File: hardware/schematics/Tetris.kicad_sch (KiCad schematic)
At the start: 13 parts, among them SW1 BTN UP, SW2 BTN RIGHT, SW3 BTN DOWN, SW4 BTN LEFT, SW5 ON/OFF Switch

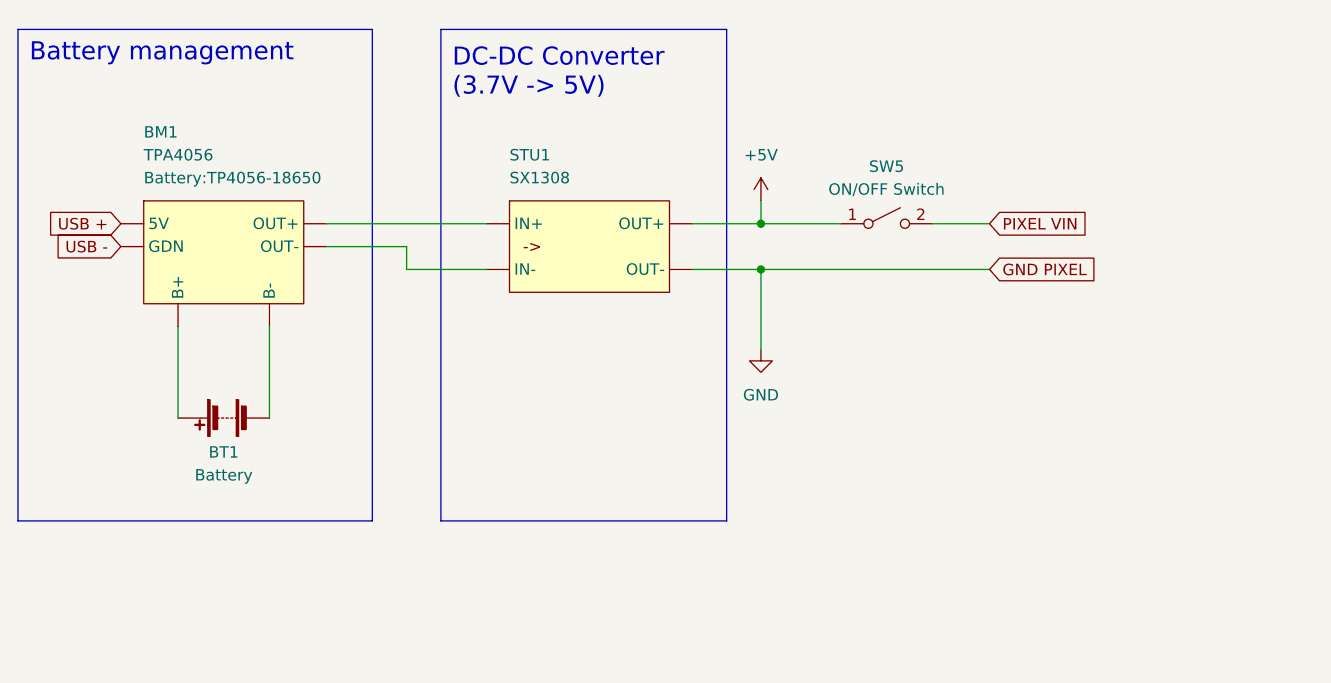
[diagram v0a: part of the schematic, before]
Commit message: Corrected schematics
Moved ON/OFF switch between battery and the DC-DC converter
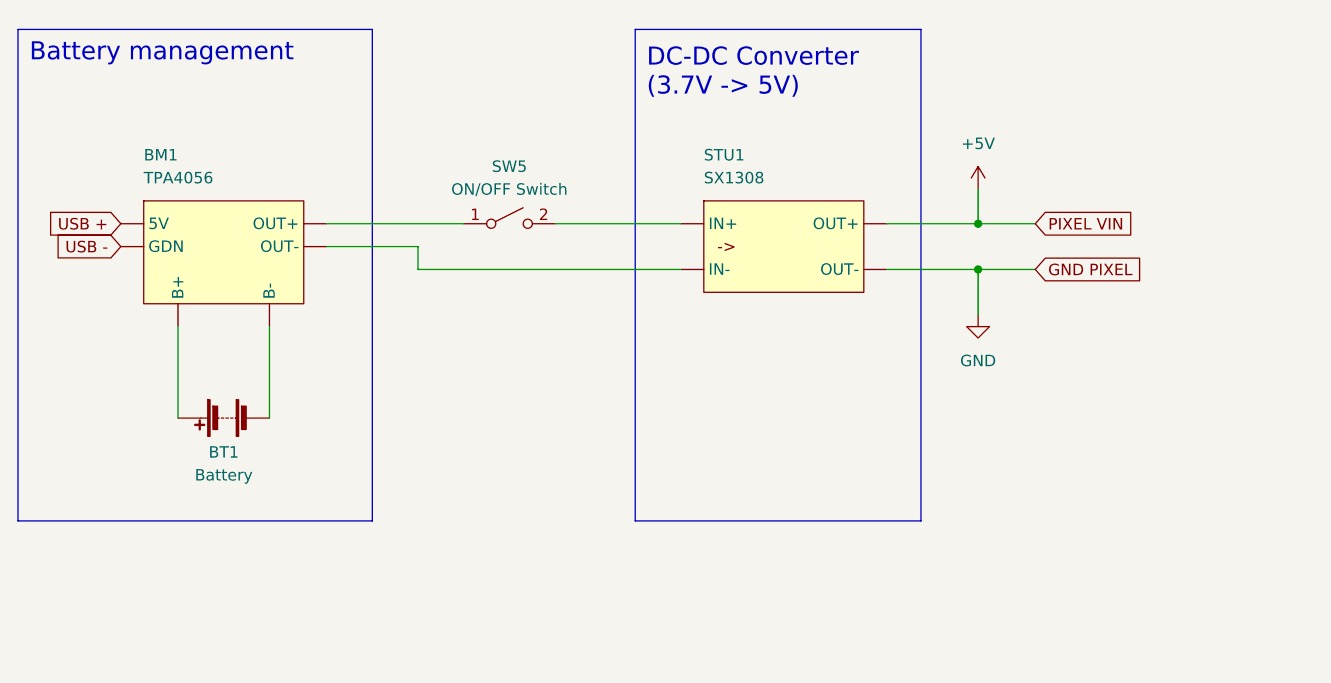
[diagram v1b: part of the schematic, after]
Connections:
- net +5V: now also DISP1. (V-); no longer SW5.1 (A)
- net at BM1.3 (OUT+): now also SW5.1 (A); no longer STU1. (OUT-)
- net PIXEL VIN: no longer names the net of SW5.2 (B)
- net PIXEL VIN: now also STU1. (OUT-); no longer DISP1. (V-)
- new net: DISP1. (V-), DISP2. (V-) (x3)
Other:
- moved on the sheet: STU1, SW5
